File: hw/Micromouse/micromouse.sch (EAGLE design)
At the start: 44 parts, among them IC1 DSPIC33FJ64MC804-PT, IC2 DRV8833PWR, J1 GP2Y0A51SK0F, J2 GP2Y0A51SK0F, J3 GP2Y0A41SK0F, SW1 B3F-1000

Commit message: Updated PCB
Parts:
- added C15, C16, C17: (no value), micromouse:CPOL_0805
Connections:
- net +5V: now also C15.+, C16.+, C17.+
- net GND: now also C15.-, C16.-, C17.-
- net S1_OUT: now also IC1.PGEC1/AN3/C2IN+/RP1/CN5/RB1; no longer IC1.AN1/VREF-/CN3/RA1
- net S3_OUT: now also IC1.AN1/VREF-/CN3/RA1; no longer IC1.PGEC1/AN3/C2IN+/RP1/CN5/RB1
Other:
- moved on the sheet: C6, C7, HDR1, HDR2, LED1, Y1

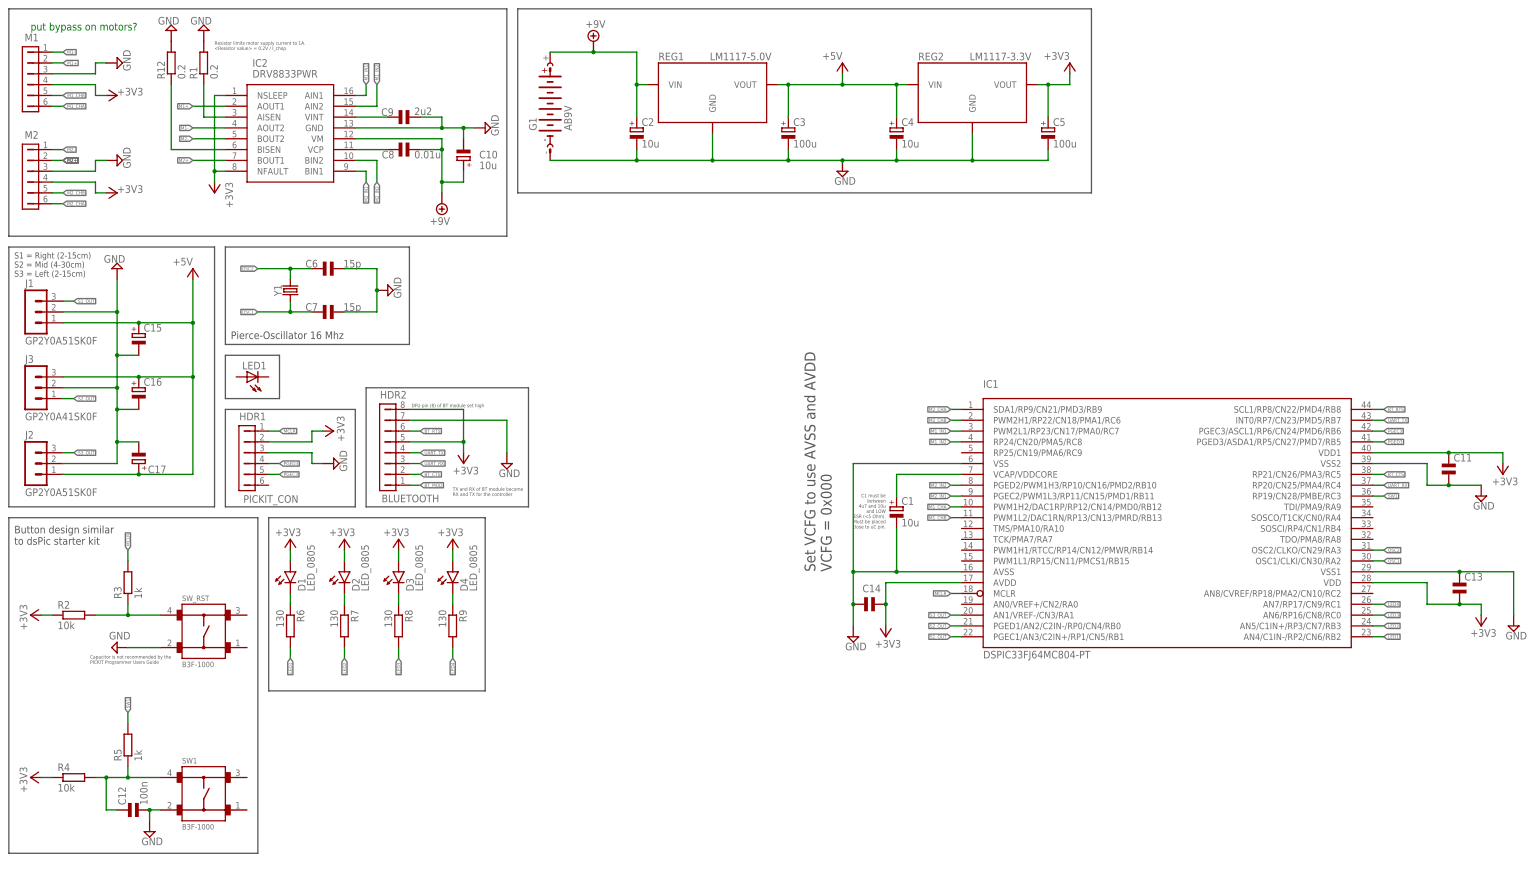
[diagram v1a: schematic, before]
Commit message: Tidied up schematic
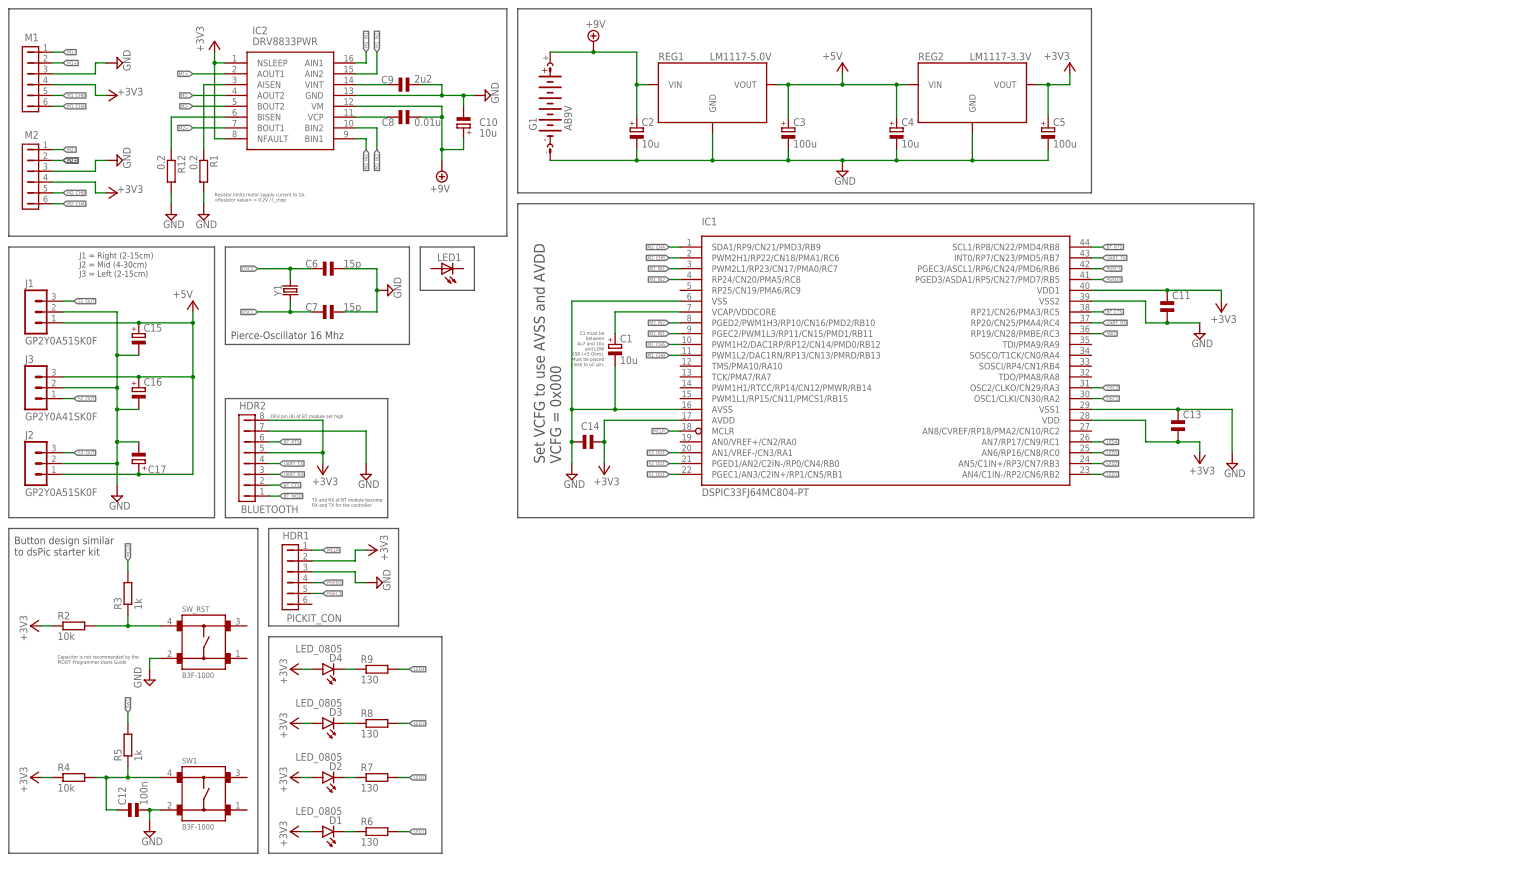
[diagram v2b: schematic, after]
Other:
- note added: "J1 = Right (2-15cm) J2 = Mid (4-30cm) J3 = Left (2-15cm)"
- note removed: "S1 = Right (2-15cm) S2 = Mid (4-30cm) S3 = Left (2-15cm)"
- note removed: "put bypass on motors?"
- moved on the sheet: C1, C10, C11, C13, C14, C8, C9, D1, D2, D3, D4, HDR1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

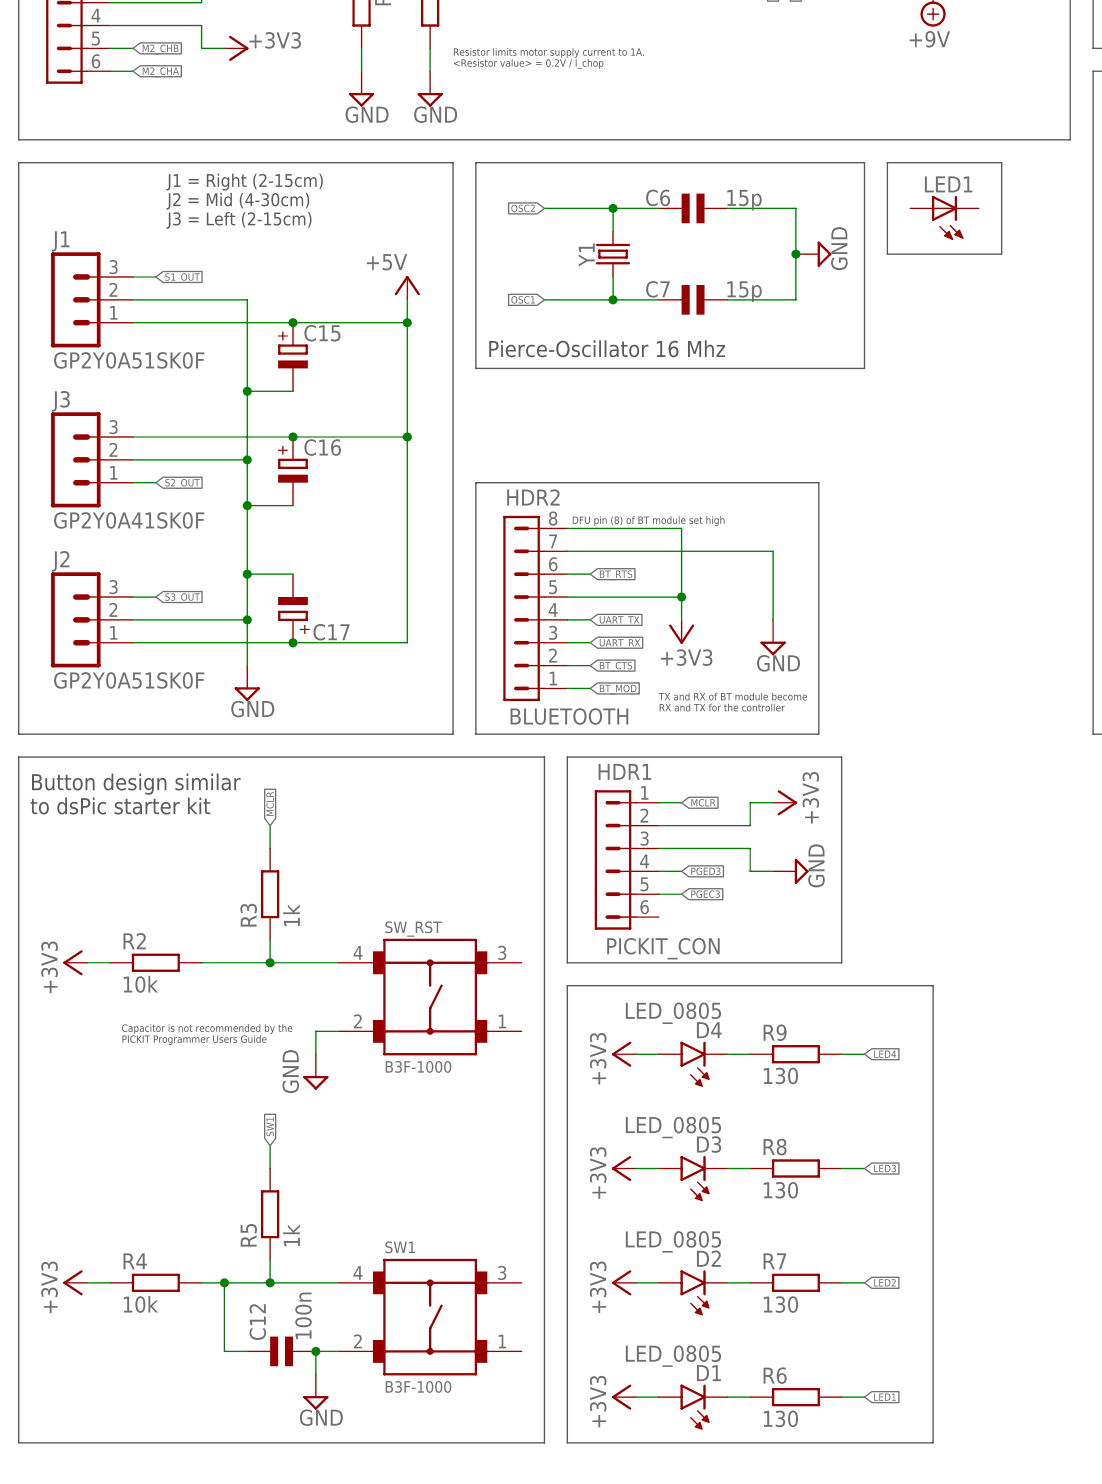
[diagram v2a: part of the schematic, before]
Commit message: Updated silkscreen
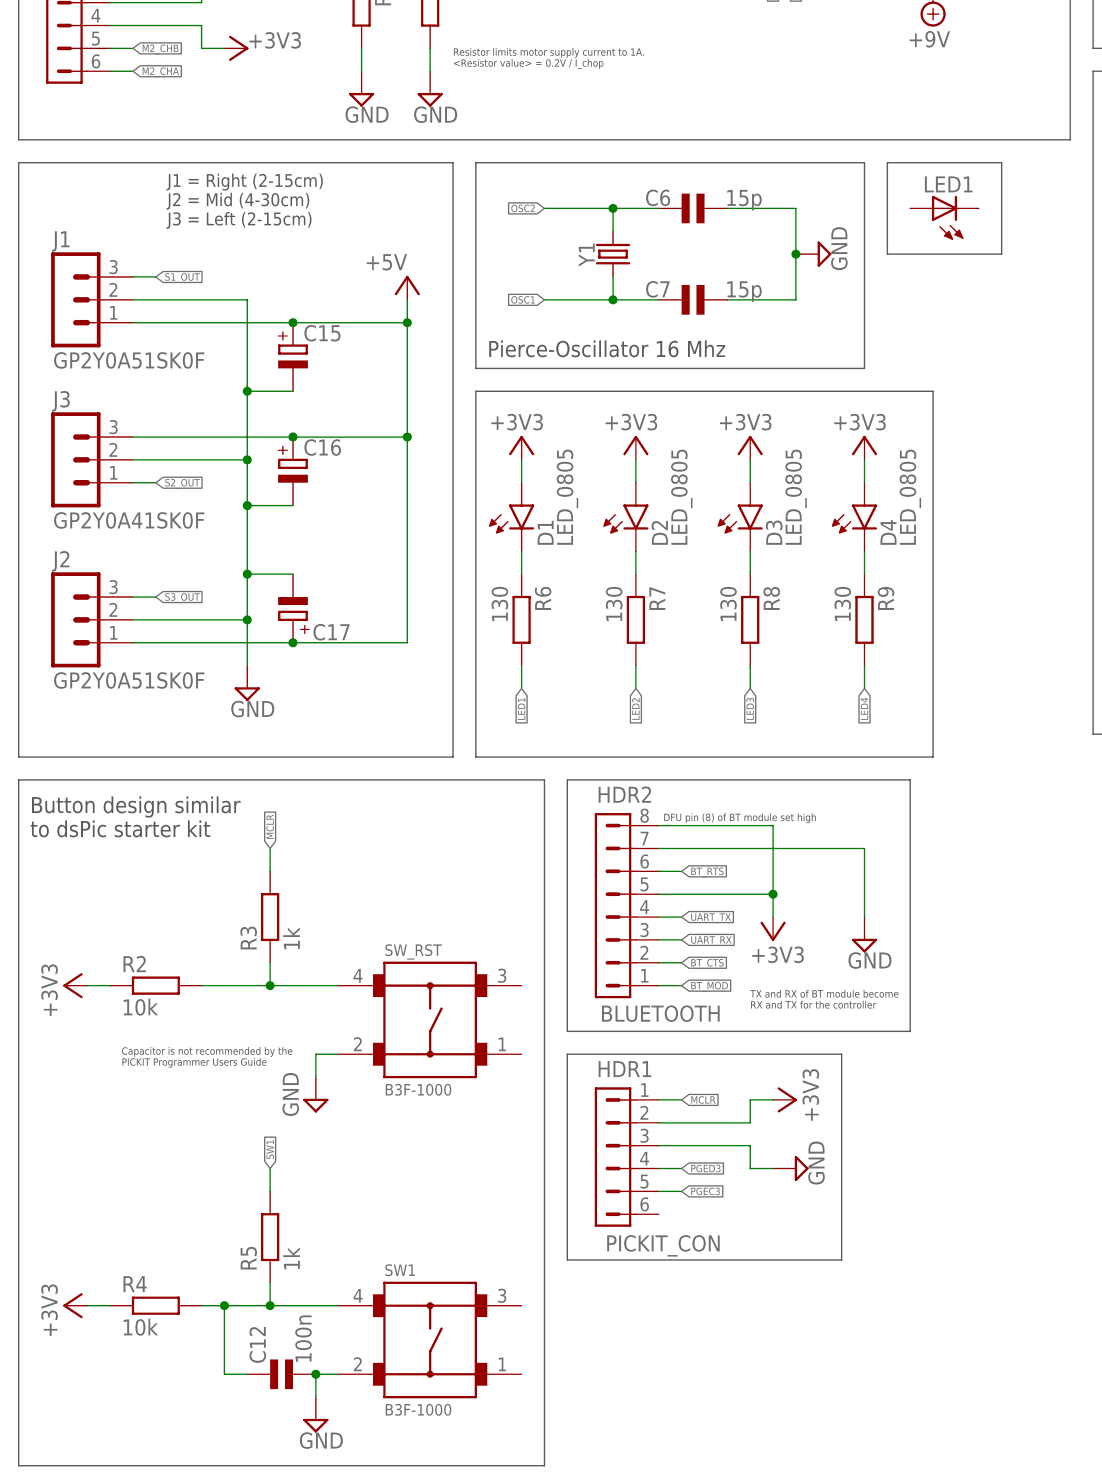
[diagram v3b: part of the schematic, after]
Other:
- moved on the sheet: C12, D1, D2, D3, D4, HDR1, HDR2, R2, R3, R4, R5, R6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

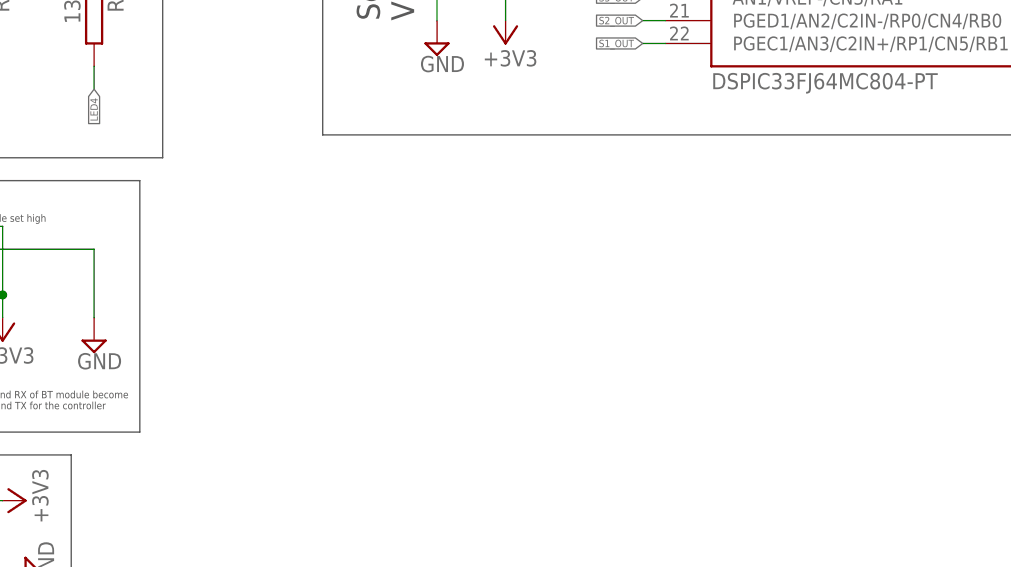
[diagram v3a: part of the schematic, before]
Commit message: Added silkscreen; Added more space between parts; Added testpoints
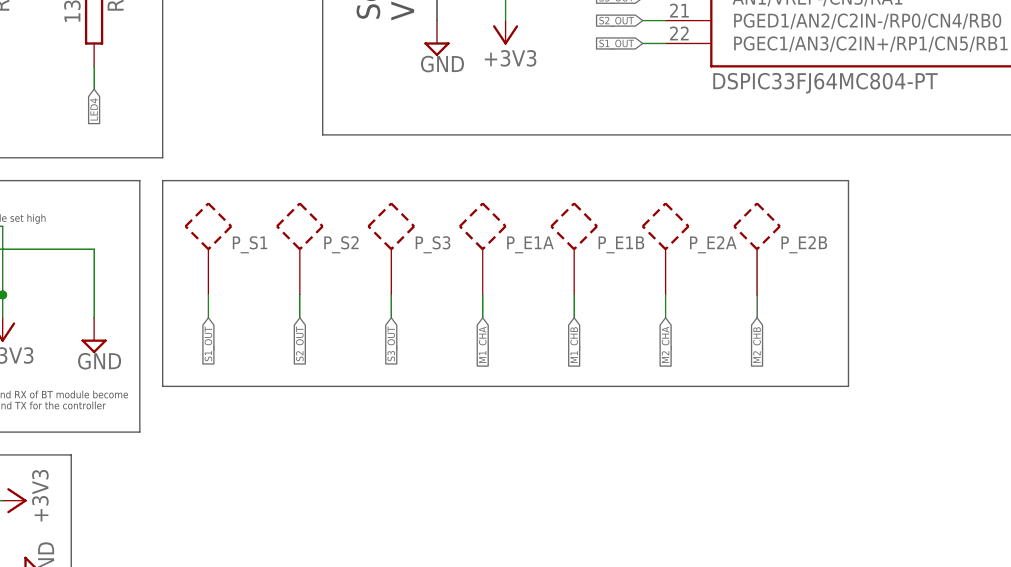
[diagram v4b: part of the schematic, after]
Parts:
- added P_E1A, P_E1B, P_E2A, P_E2B, P_S1, P_S2, P_S3: (no value), micromouse:PROBE_POINTSMD
- G1: device battery:AB9V -> micromouse:AB9V
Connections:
- net M1_CHA: now also P_E1A.P$1
- net M1_CHB: now also P_E1B.P$1
- net M2_CHA: now also P_E2A.P$1
- net M2_CHB: now also P_E2B.P$1
- net S1_OUT: now also P_S1.P$1
- net S2_OUT: now also P_S2.P$1
- net S3_OUT: now also P_S3.P$1

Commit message: Tweaked schematic and PCB
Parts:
- C11, C13, C14: value (none) -> 100n
- C15, C16, C17: value (none) -> 10u
- P_E1A, P_E1B, P_E2A, P_E2B: device micromouse:PROBE_POINTSMD -> micromouse:PROBE_POINTTHT
- R1, R12: value 0.2 -> 200m
- R6, R7, R8, R9: value 130 -> 68
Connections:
- net +3V3: no longer IC2.NFAULT
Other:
- note added: "C9 and C8 need to be low ESR ceramic"
- note added: "Vdrop = 2.2 V R = 68 Ohm I per LED = 16.18 mA"
- moved on the sheet: C12

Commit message: Added probing points for GND; Small tweaks
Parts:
- added P_GND1, P_GND2, P_GND3: (no value), micromouse:PROBE_POINTTHT
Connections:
- net GND: now also P_GND1.P$1, P_GND2.P$1, P_GND3.P$1
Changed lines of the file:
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@@
 <setting verticaltext="up"/>
 </settings>
-<grid distance="0.02" unitdist="inch" unit="inch" style="lines" multiple="1" display="no" altdistance="0.01" altunitdist="inch" altunit="inch"/>
+<grid distance="0.1" unitdist="inch" unit="inch" style="lines" multiple="1" display="no" altdistance="0.01" altunitdist="inch" altunit="inch"/>
 <layers>
 <layer number="1" name="Top" color="4" fill="1" visible="no" active="no"/>
@@
 <part name="P_E2A" library="micromouse" library_urn="urn:adsk.eagle:library:26475156" deviceset="PROBE_POINT" device="THT" package3d_urn="urn:adsk.eagle:package:26984480/2"/>
 <part name="P_E2B" library="micromouse" library_urn="urn:adsk.eagle:library:26475156" deviceset="PROBE_POINT" device="THT" package3d_urn="urn:adsk.eagle:package:26984480/2"/>
+<part name="P_GND3" library="micromouse" library_urn="urn:adsk.eagle:library:26475156" deviceset="PROBE_POINT" device="THT" package3d_urn="urn:adsk.eagle:package:26984480/2"/>
+<part name="SUPPLY14" library="supply2" library_urn="urn:adsk.eagle:library:372" deviceset="GND" device=""/>
+<part name="P_GND1" library="micromouse" library_urn="urn:adsk.eagle:library:26475156" deviceset="PROBE_POINT" device="THT" package3d_urn="urn:adsk.eagle:package:26984480/2"/>
+<part name="SUPPLY15" library="supply2" library_urn="urn:adsk.eagle:library:372" deviceset="GND" device=""/>
+<part name="P_GND2" library="micromouse" library_urn="urn:adsk.eagle:library:26475156" deviceset="PROBE_POINT" device="THT" package3d_urn="urn:adsk.eagle:package:26984480/2"/>
+<part name="SUPPLY16" library="supply2" library_urn="urn:adsk.eagle:library:372" deviceset="GND" device=""/>
 </parts>
 <sheets>
@@
 <wire x1="147.32" y1="55.88" x2="-25.4" y2="55.88" width="0.1524" layer="97"/>
 <wire x1="-43.18" y1="-22.86" x2="-43.18" y2="-45.72" width="0.1524" layer="97"/>
-<wire x1="-43.18" y1="-45.72" x2="33.02" y2="-45.72" width="0.1524" layer="97"/>
-<wire x1="33.02" y1="-45.72" x2="33.02" y2="-22.86" width="0.1524" layer="97"/>
-<wire x1="33.02" y1="-22.86" x2="-43.18" y2="-22.86" width="0.1524" layer="97"/>
+<wire x1="-43.18" y1="-45.72" x2="71.12" y2="-45.72" width="0.1524" layer="97"/>
+<wire x1="71.12" y1="-45.72" x2="71.12" y2="-22.86" width="0.1524" layer="97"/>
+<wire x1="71.12" y1="-22.86" x2="-43.18" y2="-22.86" width="0.1524" layer="97"/>
 <text x="-55.372" y="72.644" size="0.8128" layer="97" align="top-left">C9 and C8 need to
 be low ESR ceramic</text>
@@
 <attribute name="NAME" x="25.4" y="-30.48" size="1.4224" layer="95"/>
 <attribute name="VALUE" x="25.4" y="-35.56" size="1.4224" layer="96"/>
+</instance>
+<instance part="P_GND3" gate="G$1" x="58.42" y="-30.48" smashed="yes">
+<attribute name="NAME" x="60.96" y="-30.48" size="1.4224" layer="95"/>
+<attribute name="VALUE" x="60.96" y="-35.56" size="1.4224" layer="96"/>
+</instance>
+<instance part="SUPPLY14" gate="GND" x="58.42" y="-40.64" smashed="yes">
+<attribute name="VALUE" x="56.515" y="-43.815" size="1.778" layer="96"/>
+</instance>
+<instance part="P_GND1" gate="G$1" x="33.02" y="-30.48" smashed="yes">
+<attribute name="NAME" x="35.56" y="-30.48" size="1.4224" layer="95"/>
+<attribute name="VALUE" x="35.56" y="-35.56" size="1.4224" layer="96"/>
+</instance>
+<instance part="SUPPLY15" gate="GND" x="33.02" y="-40.64" smashed="yes">
+<attribute name="VALUE" x="31.115" y="-43.815" size="1.778" layer="96"/>
+</instance>
+<instance part="P_GND2" gate="G$1" x="45.72" y="-30.48" smashed="yes">
+<attribute name="NAME" x="48.26" y="-30.48" size="1.4224" layer="95"/>
+<attribute name="VALUE" x="48.26" y="-35.56" size="1.4224" layer="96"/>
+</instance>
+<instance part="SUPPLY16" gate="GND" x="45.72" y="-40.64" smashed="yes">
+<attribute name="VALUE" x="43.815" y="-43.815" size="1.778" layer="96"/>
 </instance>
 </instances>
@@
 <junction x="-110.744" y="-88.9"/>
 </segment>
+<segment>
+<pinref part="P_GND3" gate="G$1" pin="P$1"/>
+<wire x1="58.42" y1="-35.56" x2="58.42" y2="-38.1" width="0.1524" layer="91"/>
+<pinref part="SUPPLY14" gate="GND" pin="GND"/>
+</segment>
+<segment>
+<pinref part="P_GND1" gate="G$1" pin="P$1"/>
+<wire x1="33.02" y1="-35.56" x2="33.02" y2="-38.1" width="0.1524" layer="91"/>
+<pinref part="SUPPLY15" gate="GND" pin="GND"/>
+</segment>
+<segment>
+<pinref part="P_GND2" gate="G$1" pin="P$1"/>
+<wire x1="45.72" y1="-35.56" x2="45.72" y2="-38.1" width="0.1524" layer="91"/>
+<pinref part="SUPPLY16" gate="GND" pin="GND"/>
+</segment>
 </net>
